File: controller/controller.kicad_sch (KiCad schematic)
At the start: 82 parts, among them J11 Conn_ARM_JTAG_SWD_10, J12 GRPB072VWQS-RC, J13 GRPB072VWQS-RC, J14 Conn_01x03_Pin, J6 USB_C_Receptacle_USB2.0_16P, J7 USB_C_Receptacle_USB2.0_16P, J8 GRPB072VWQS-RC, J9 GRPB072VWQS-RC, SW3 Boot, SW4 Reset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

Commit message: Controller - Some changes
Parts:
- added C41, C42, C43, C44, C45, C61, C62: 100nF, Capacitor_SMD:C_0402_1005Metric, symbol Device:C_Small
- added Q1, Q2: BSS138, Package_TO_SOT_SMD:SOT-23, symbol Transistor_FET:BSS138
- added R25, R26: ?k, Resistor_SMD:R_0402_1005Metric, symbol Device:R_Small
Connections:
- net +5V: now also C41.1, C42.1, C43.1, C44.1, C45.1, C61.1, C62.1, R25.2, R26.2
- net CC1_MCU: no longer J12.9 (Pin_9)
- net CC2_MCU: no longer J12.7 (Pin_7)
- net Earth: now also C41.2, C42.2, C43.2, C44.2, C45.2, C61.2, C62.2, Q1.2 (S), Q2.2 (S)
- net LED_CH1: now also Q1.3 (D), R25.1
- net LED_CH2: now also Q2.3 (D), R26.1
- net OTHER_USB_CC1: now also J12.9 (Pin_9); no longer J9.8 (Pin_8)
- net OTHER_USB_CC2: now also J12.7 (Pin_7); no longer J9.6 (Pin_6)
- new net esp32c6/LED_CH1: Q1.1 (G)
- new net esp32c6/LED_CH2: Q2.1 (G)
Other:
- moved on the sheet: J12

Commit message: Controller - Some changes
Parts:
- added C63: 100nF, Capacitor_SMD:C_0402_1005Metric, symbol Device:C_Small
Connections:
- net +3V3: now also C63.1
- net CC1_MCU: now also J9.8 (Pin_8)
- net CC2_MCU: now also J9.6 (Pin_6)
- net Earth: now also C63.2
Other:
- moved on the sheet: J9

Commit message: Controller - More routing
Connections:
- net +3V3: now also J8.10 (Pin_10); no longer J8.9 (Pin_9)
- net 6-18V: now also J8.9 (Pin_9); no longer J8.10 (Pin_10)
- net Earth: now also J8.4 (Pin_4); no longer J8.3 (Pin_3)
- net VBUS1: now also J8.3 (Pin_3); no longer J8.4 (Pin_4)
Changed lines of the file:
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@@
 	)
 	(junction
+		(at 76.2 325.12)
+		(diameter 0)
+		(color 0 0 0 0)
+	)
+	(junction
 		(at 207.01 113.03)
 		(diameter 0)
@@
 	)
 	(junction
-		(at 63.5 325.12)
-		(diameter 0)
-		(color 0 0 0 0)
-	)
-	(junction
 		(at 149.86 44.45)
 		(diameter 0)
@@
 	(wire
 		(pts
-			(xy 63.5 322.58) (xy 63.5 325.12)
-		)
-		(stroke
-			(width 0)
-			(type default)
-		)
-	)
-	(wire
-		(pts
 			(xy 236.22 270.51) (xy 236.22 275.59)
 		)
@@
 	(wire
 		(pts
-			(xy 63.5 314.96) (xy 50.8 314.96)
+			(xy 76.2 314.96) (xy 82.55 314.96)
 		)
 		(stroke
@@
 	(wire
 		(pts
-			(xy 77.47 314.96) (xy 76.2 314.96)
-		)
-		(stroke
-			(width 0)
-			(type default)
-		)
-	)
-	(wire
-		(pts
 			(xy 251.46 198.12) (xy 264.16 198.12)
 		)
@@
 	(wire
 		(pts
+			(xy 76.2 322.58) (xy 76.2 325.12)
+		)
+		(stroke
+			(width 0)
+			(type default)
+		)
+	)
+	(wire
+		(pts
 			(xy 44.45 229.87) (xy 106.68 229.87)
 		)
@@
 	(wire
 		(pts
-			(xy 78.74 322.58) (xy 76.2 322.58)
+			(xy 60.96 322.58) (xy 63.5 322.58)
 		)
 		(stroke
@@
 	(wire
 		(pts
+			(xy 58.42 314.96) (xy 63.5 314.96)
+		)
+		(stroke
+			(width 0)
+			(type default)
+		)
+	)
+	(wire
+		(pts
 			(xy 509.27 151.13) (xy 513.08 151.13)
 		)
@@
 	(global_label "6-18V"
 		(shape input)
-		(at 50.8 314.96 180)
+		(at 82.55 314.96 0)
 		(fields_autoplaced yes)
 		(effects
@@
 				(size 1.27 1.27)
 			)
-			(justify right)
+			(justify left)
 		)
 		(property "Intersheetrefs" "${INTERSHEET_REFS}"
-			(at 41.5253 314.96 0)
+			(at 91.8247 314.96 0)
 			(effects
 				(font
 					(size 1.27 1.27)
 				)
-				(justify right)
+				(justify left)
 				(hide yes)
 			)
@@
 	(symbol
 		(lib_id "power:Earth")
-		(at 78.74 322.58 0)
-		(mirror y)
+		(at 60.96 322.58 0)
 		(unit 1)
 		(exclude_from_sim no)
@@
 		(fields_autoplaced yes)
 		(property "Reference" "#PWR086"
-			(at 78.74 328.93 0)
+			(at 60.96 328.93 0)
 			(effects
 				(font
@@
 		)
 		(property "Value" "Earth"
-			(at 78.74 326.39 0)
+			(at 60.96 326.39 0)
 			(effects
 				(font
@@
 		)
 		(property "Footprint" ""
-			(at 78.74 322.58 0)
+			(at 60.96 322.58 0)
 			(effects
 				(font
@@
 		)
 		(property "Datasheet" "~"
-			(at 78.74 322.58 0)
+			(at 60.96 322.58 0)
 			(effects
 				(font
@@
 		)
 		(property "Description" ""
-			(at 78.74 322.58 0)
+			(at 60.96 322.58 0)
 			(effects
 				(font
@@
 	(symbol
 		(lib_id "power:+3V3")
-		(at 77.47 314.96 0)
+		(at 58.42 314.96 0)
 		(mirror y)
 		(unit 1)
@@
 		(fields_autoplaced yes)
 		(property "Reference" "#PWR036"
-			(at 77.47 318.77 0)
+			(at 58.42 318.77 0)
 			(effects
 				(font
@@
 		)
 		(property "Value" "+3V3"
-			(at 77.47 311.15 0)
+			(at 58.42 311.15 0)
 			(effects
 				(font
@@
 		)
 		(property "Footprint" ""
-			(at 77.47 314.96 0)
+			(at 58.42 314.96 0)
 			(effects
 				(font
@@
 		)
 		(property "Datasheet" ""
-			(at 77.47 314.96 0)
+			(at 58.42 314.96 0)
 			(effects
 				(font
@@
 		)
 		(property "Description" "Power symbol creates a global label with name \"+3V3\""
-			(at 77.47 314.96 0)
+			(at 58.42 314.96 0)
 			(effects
 				(font

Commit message: Controller - Most things routed
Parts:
- removed C30: 10nF, Capacitor_SMD:C_0402_1005Metric, symbol Device:C_Small
- removed J14: Conn_01x03_Pin, Connector_PinHeader_2.54mm:PinHeader_1x03_P2.54mm_Vertical_SMD_Pin1Left, symbol Connector:Conn_01x03_Pin
- added C64: 10uF, Capacitor_SMD:C_0805_2012Metric, symbol Device:C_Small
- added C65: 100nF, Capacitor_SMD:C_0402_1005Metric, symbol Device:C_Small
- added J15: Conn_01x03_Pin, Connector_PinHeader_2.54mm:PinHeader_1x03_P2.54mm_Vertical_SMD_Pin1Left, symbol Connector:Conn_01x03_Pin
- R28: footprint Resistor_SMD:R_0402_1005Metric -> Resistor_SMD:R_0603_1608Metric
- RV3: footprint (none) -> Potentiometer_THT:Potentiometer_Alps_RK09Y11_Single_Horizontal
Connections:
- net +3V3: now also C64.1
- net +5V: now also C65.1, J15.3 (Pin_3)
- net Current_sense_5: no longer R28.1
- net Earth: now also C64.2, C65.2, J15.2 (Pin_2)
- net LED_CH2: now also J15.1 (Pin_1)
- net STM32_NRST: now also R28.1; no longer C19.1, U1.7 (PG10)
- net pwm_led4: no longer U1.30 (PB10)
- net POWER_BTN: now reaches C40.1, R118.1
- net POWER_BTN: now also U1.30 (PB10); no longer U1.4 (PC15)
- net at R28.2: now also C19.1, U1.7 (PG10)
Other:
- moved on the sheet: C40, R118, R69, R70, R72, R73, SW4, SW5, U8

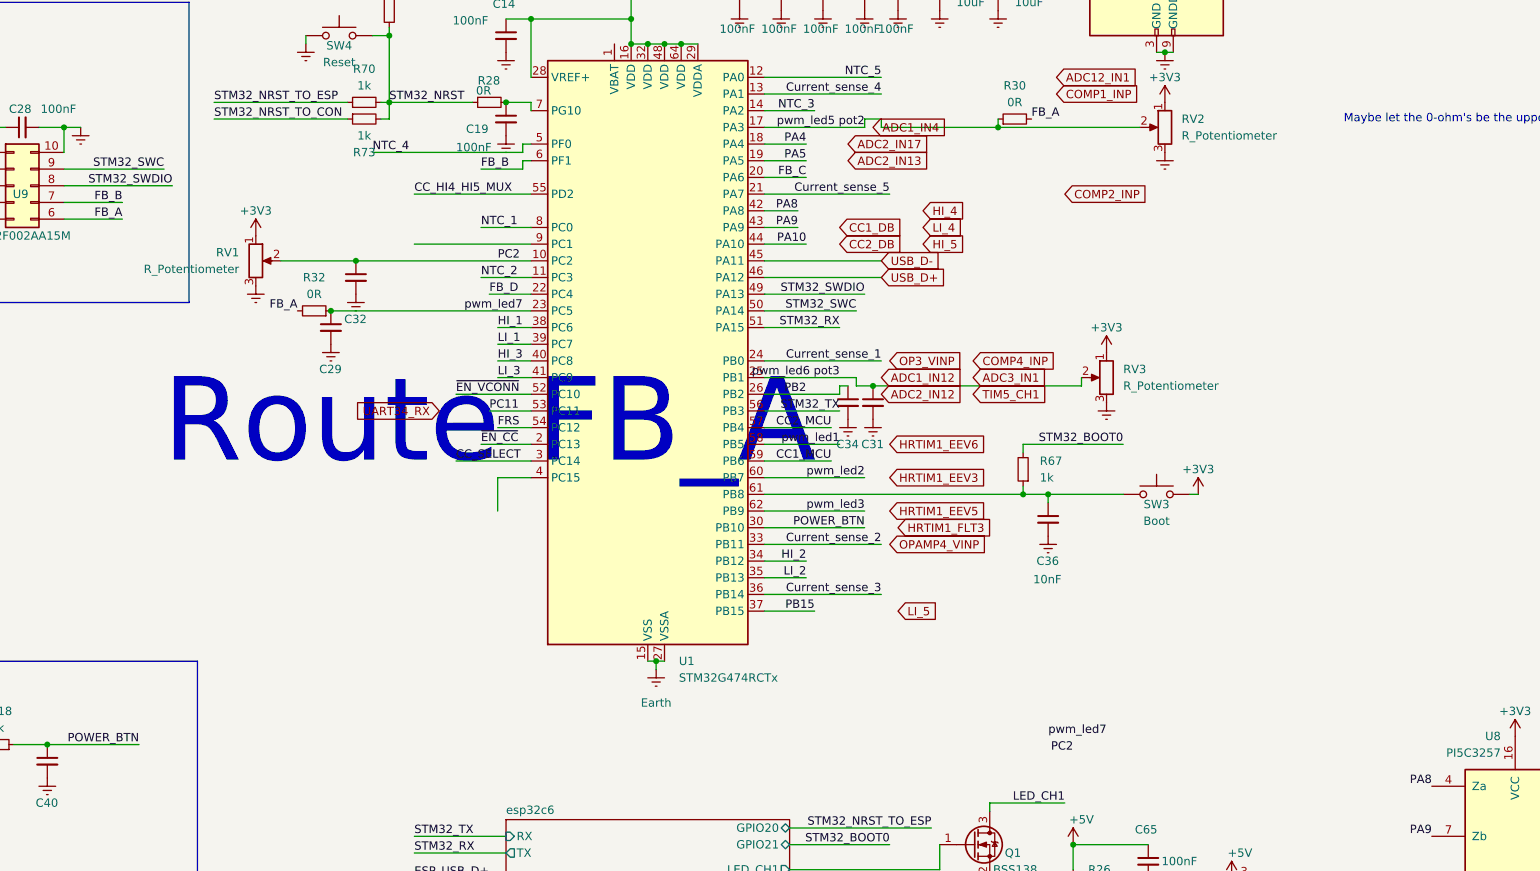
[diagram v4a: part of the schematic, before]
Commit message: Controller - Add rotary encoder
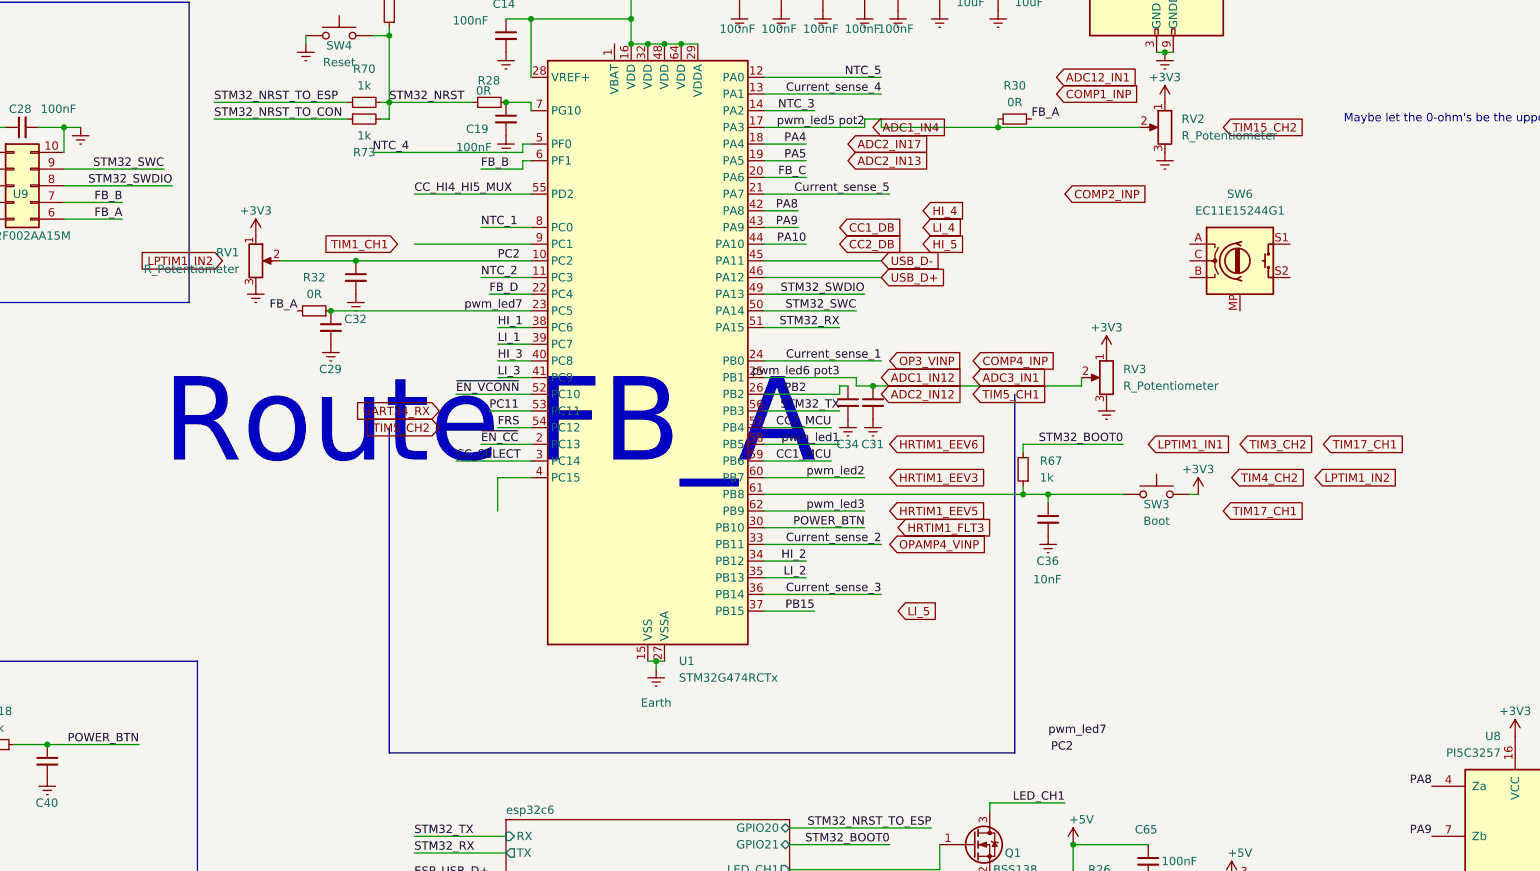
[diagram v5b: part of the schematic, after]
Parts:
- added SW6: EC11E15244G1, Rotary_Encoder:RotaryEncoder_Alps_EC11E-Switch_Vertical_H20mm_CircularMountingHoles, symbol Device:RotaryEncoder_Switch_MP
- RV1: footprint (none) -> Potentiometer_THT:Potentiometer_Alps_RK09Y11_Single_Horizontal
- RV2: footprint (none) -> Rotary_Encoder:RotaryEncoder_Alps_EC12E_Vertical_H20mm
- SW3: footprint (none) -> Button_Switch_SMD:SW_SPST_PTS647_Sx50

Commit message: Controller - More work around rotary encoder and move protection diodes
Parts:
- removed U12: QSBT40-7-F, Package_TO_SOT_SMD:SOT-363_SC-70-6, symbol Library:QSBT40-7-F
- added C30: 1uF, Capacitor_SMD:C_0402_1005Metric, symbol Device:C_Small
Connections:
- net +3V3: now also C30.2
- net Earth: now also SW6.C, SW6.MP, SW6.S2, C30.1
- net FB_A: now also U13.3 (DL3); no longer U14.6 (DL1)
- net FB_B: now also U14.6 (DL1); no longer U14.1 (DL4)
- net FB_C: now also U13.6 (DL1); no longer U13.1 (DL4)
- net FB_D: now also U14.1 (DL4); no longer U13.6 (DL1)
- net NTC_2: now also U14.4 (DL2)
- net NTC_3: now also U14.3 (DL3)
- net PA5: now also U13.1 (DL4); no longer U13.3 (DL3)
- net pwm_led1: now also SW6.A
- net pwm_led2: now also SW6.B
- net pwm_led3: now also SW6.S1
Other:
- note removed: "Maybe let the 0-ohm's be the upper half of the dividers?"
- moved on the sheet: U13A, U13C, U13D, U14A, U14B, U14C, U14D

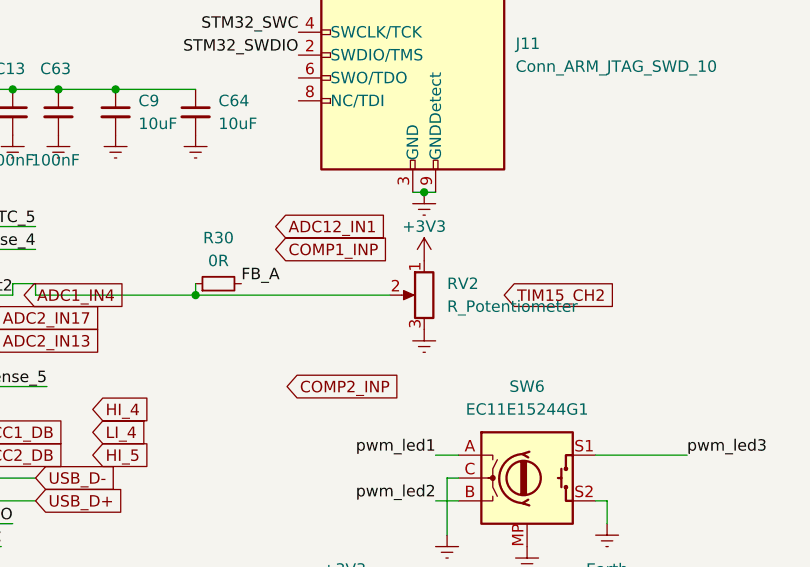
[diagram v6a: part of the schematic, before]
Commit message: Controller - Fix all DRC errors and some warnings
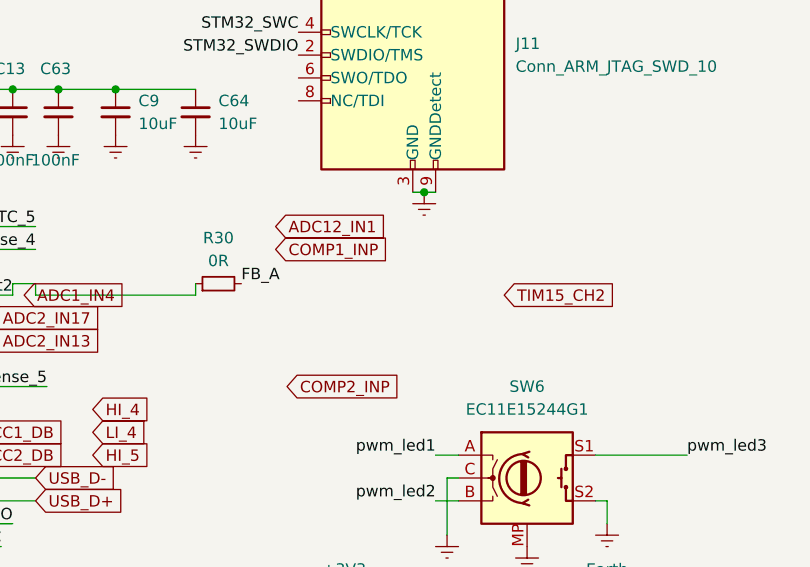
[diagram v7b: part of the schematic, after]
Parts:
- removed RV2: R_Potentiometer, Rotary_Encoder:RotaryEncoder_Alps_EC12E_Vertical_H20mm, symbol Device:R_Potentiometer
- R19, R20, R21, R22: footprint (none) -> Resistor_SMD:R_0402_1005Metric
- SW3: footprint Button_Switch_SMD:SW_SPST_PTS647_Sx50 -> Button_Switch_SMD:SW_SPST_B3U-1000P
- SW4: footprint (none) -> Button_Switch_SMD:SW_SPST_B3U-1000P
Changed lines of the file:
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@@
 	)
 	(junction
-		(at 203.2 57.15)
-		(diameter 0)
-		(color 0 0 0 0)
-	)
-	(junction
 		(at 163.83 34.29)
 		(diameter 0)
@@
 	(wire
 		(pts
-			(xy 224.79 57.15) (xy 203.2 57.15)
-		)
-		(stroke
-			(width 0)
-			(type default)
-		)
-	)
-	(wire
-		(pts
 			(xy 128.27 40.64) (xy 132.08 40.64)
 		)
@@
 			)
 		)
-		(property "Footprint" ""
+		(property "Footprint" "Resistor_SMD:R_0402_1005Metric"
 			(at 101.6 233.68 0)
 			(effects
@@
 			)
 		)
-		(property "Footprint" "Button_Switch_SMD:SW_SPST_PTS647_Sx50"
+		(property "Footprint" "Button_Switch_SMD:SW_SPST_B3U-1000P"
 			(at 227.33 107.95 0)
 			(effects
@@
 			)
 		)
-		(property "Footprint" ""
+		(property "Footprint" "Button_Switch_SMD:SW_SPST_B3U-1000P"
 			(at 102.87 38.1 0)
 			(effects
@@
 			)
 		)
-		(property "Footprint" ""
+		(property "Footprint" "Resistor_SMD:R_0402_1005Metric"
 			(at 106.68 224.79 0)
 			(effects
@@
 			)
 		)
-		(property "Footprint" ""
+		(property "Footprint" "Resistor_SMD:R_0402_1005Metric"
 			(at 101.6 224.79 0)
 			(effects
@@
 	)
 	(symbol
-		(lib_id "Device:R_Potentiometer")
-		(at 228.6 57.15 0)
-		(mirror y)
-		(unit 1)
-		(exclude_from_sim no)
-		(in_bom yes)
-		(on_board yes)
-		(dnp no)
-		(fields_autoplaced yes)
-		(property "Reference" "RV2"
-			(at 231.14 55.8799 0)
-			(effects
-				(font
-					(size 1.27 1.27)
-				)
-				(justify right)
-			)
-		)
-		(property "Value" "R_Potentiometer"
-			(at 231.14 58.4199 0)
-			(effects
-				(font
-					(size 1.27 1.27)
-				)
-				(justify right)
-			)
-		)
-		(property "Footprint" "Rotary_Encoder:RotaryEncoder_Alps_EC12E_Vertical_H20mm"
-			(at 228.6 57.15 0)
-			(effects
-				(font
-					(size 1.27 1.27)
-				)
-				(hide yes)
-			)
-		)
-		(property "Datasheet" "~"
-			(at 228.6 57.15 0)
-			(effects
-				(font
-					(size 1.27 1.27)
-				)
-				(hide yes)
-			)
-		)
-		(property "Description" "Potentiometer"
-			(at 228.6 57.15 0)
-			(effects
-				(font
-					(size 1.27 1.27)
-				)
-				(hide yes)
-			)
-		)
-		(pin "3"
-		)
-		(pin "2"
-		)
-		(pin "1"
-		)
-		(instances
-			(project "controller"
-				(path "/5b092a03-7e3e-4df1-ad91-2ac0e362f857"
-					(reference "RV2")
-					(unit 1)
-				)
-			)
-		)
-	)
-	(symbol
 		(lib_id "Device:C_Small")
 		(at 346.71 153.67 0)
@@
 	)
 	(symbol
-		(lib_id "power:+3V3")
-		(at 228.6 53.34 0)
-		(mirror y)
-		(unit 1)
-		(exclude_from_sim no)
-		(in_bom yes)
-		(on_board yes)
-		(dnp no)
-		(fields_autoplaced yes)
-		(property "Reference" "#PWR068"
-			(at 228.6 57.15 0)
-			(effects
-				(font
-					(size 1.27 1.27)
-				)
-				(hide yes)
-			)
-		)
-		(property "Value" "+3V3"
-			(at 228.6 49.53 0)
-			(effects
-				(font
-					(size 1.27 1.27)
-				)
-			)
-		)
-		(property "Footprint" ""
-			(at 228.6 53.34 0)
-			(effects
-				(font
-					(size 1.27 1.27)
-				)
-				(hide yes)
-			)
-		)
-		(property "Datasheet" ""
-			(at 228.6 53.34 0)
-			(effects
-				(font
-					(size 1.27 1.27)
-				)
-				(hide yes)
-			)
-		)
-		(property "Description" "Power symbol creates a global label with name \"+3V3\""
-			(at 228.6 53.34 0)
-			(effects
-				(font
-					(size 1.27 1.27)
-				)
-				(hide yes)
-			)
-		)
-		(pin "1"
-		)
-		(instances
-			(project "controller"
-				(path "/5b092a03-7e3e-4df1-ad91-2ac0e362f857"
-					(reference "#PWR068")
-					(unit 1)
-				)
-			)
-		)
-	)
-	(symbol
 		(lib_id "power:Earth")
 		(at 128.27 58.42 0)
@@
 	)
 	(symbol
-		(lib_id "power:Earth")
-		(at 228.6 60.96 0)
-		(mirror y)
-		(unit 1)
-		(exclude_from_sim no)
-		(in_bom yes)
-		(on_board yes)
-		(dnp no)
-		(fields_autoplaced yes)
-		(property "Reference" "#PWR073"
-			(at 228.6 67.31 0)
-			(effects
-				(font
-					(size 1.27 1.27)
-				)
-				(hide yes)
-			)
-		)
-		(property "Value" "Earth"
-			(at 228.6 66.04 0)
-			(effects
-				(font
-					(size 1.27 1.27)
-				)
-				(hide yes)
-			)
-		)
-		(property "Footprint" ""
-			(at 228.6 60.96 0)
-			(effects
-				(font
-					(size 1.27 1.27)
-				)
-				(hide yes)
-			)
-		)
-		(property "Datasheet" "~"
-			(at 228.6 60.96 0)
-			(effects
-				(font
-					(size 1.27 1.27)
-				)
-				(hide yes)
-			)
-		)
-		(property "Description" "Power symbol creates a global label with name \"Earth\""
-			(at 228.6 60.96 0)
-			(effects
-				(font
-					(size 1.27 1.27)
-				)
-				(hide yes)
-			)
-		)
-		(pin "1"
-		)
-		(instances
-			(project "controller"
-				(path "/5b092a03-7e3e-4df1-ad91-2ac0e362f857"
-					(reference "#PWR073")
-					(unit 1)
-				)
-			)
-		)
-	)
-	(symbol
 		(lib_id "Device:C_Small")
 		(at 370.84 270.51 0)
@@
 			)
 		)
-		(property "Footprint" ""
+		(property "Footprint" "Resistor_SMD:R_0402_1005Metric"
 			(at 106.68 233.68 0)
 			(effects
